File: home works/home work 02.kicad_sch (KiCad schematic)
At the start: 4 parts, among them U1 AW9523B, U2 XS2184, U3 BL0910, U4 HLK-7628N

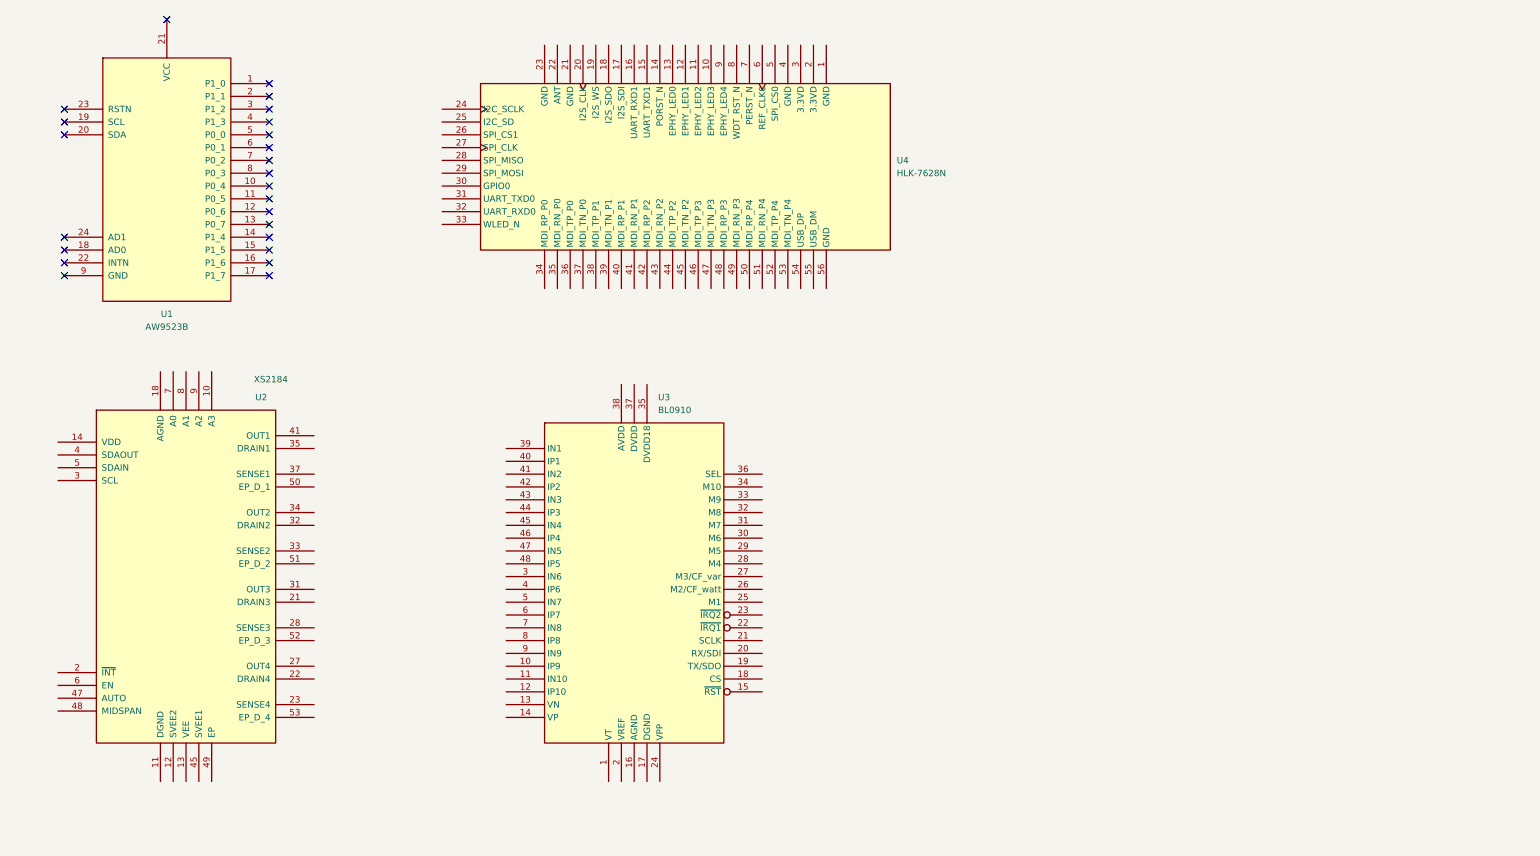
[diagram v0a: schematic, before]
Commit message: update schemas structure
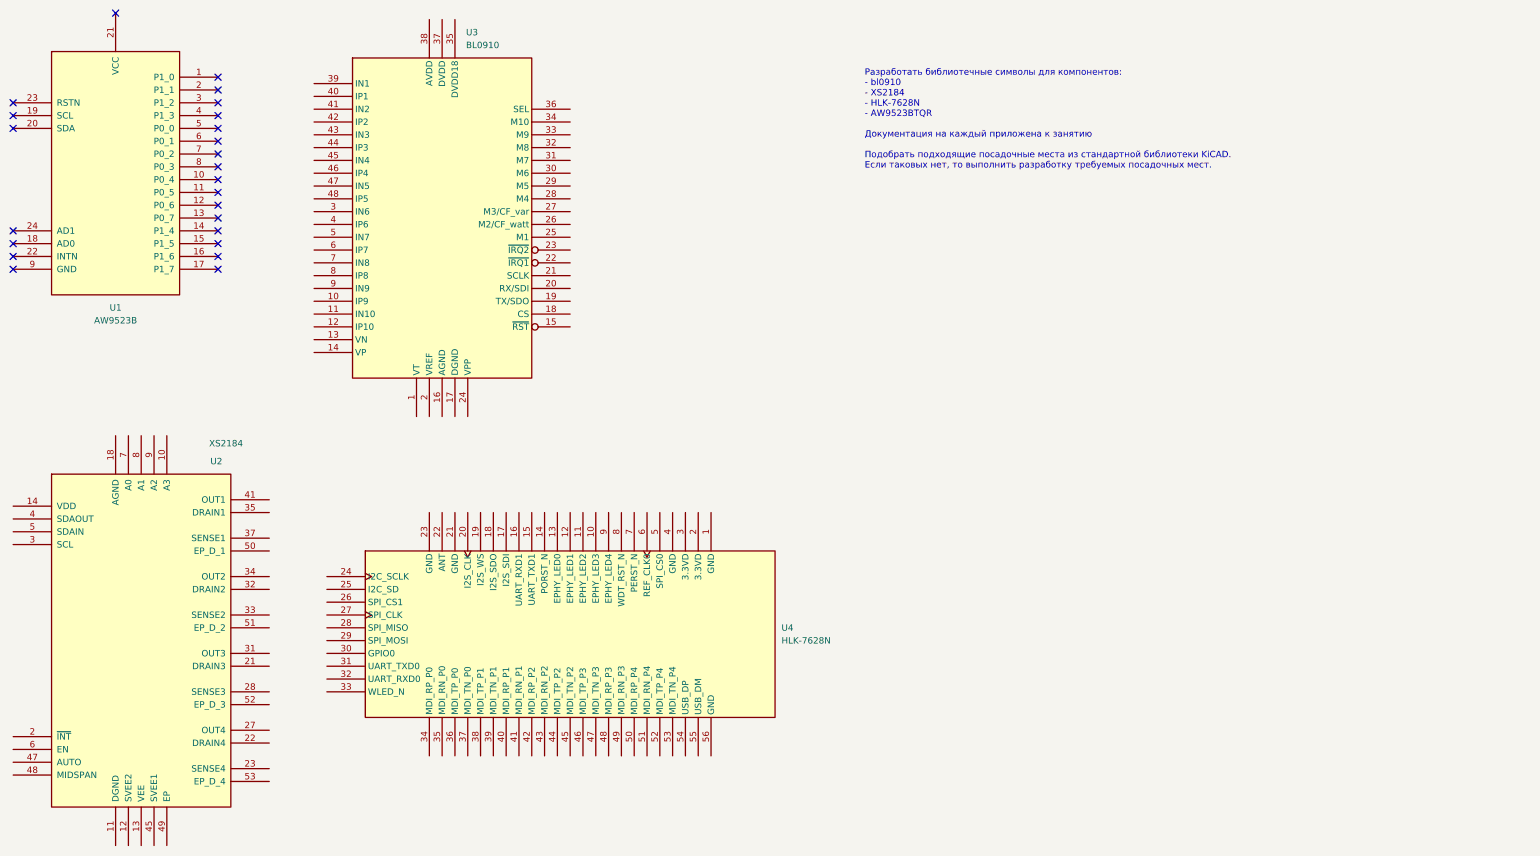
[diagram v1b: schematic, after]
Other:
- note added: "Разработать библиотечные символы для компонентов: - bl0910 - XS2184 - HLK-7628N - AW9523BTQR Документация на каждый приложена к занятию Подобрать подходящие посадочные места из стандартной библиотеки KiCAD. Если таковых нет, то выполнить разработку требуемых посадочных мест."
- moved on the sheet: U1, U2, U3, U4
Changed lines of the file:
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@@
 	(paper "A4")
 	(no_connect
-		(at 71.12 66.04)
-	)
-	(no_connect
-		(at 71.12 53.34)
-	)
-	(no_connect
-		(at 30.48 71.12)
-	)
-	(no_connect
-		(at 71.12 55.88)
-	)
-	(no_connect
-		(at 71.12 35.56)
-	)
-	(no_connect
-		(at 50.8 20.32)
-	)
-	(no_connect
-		(at 30.48 40.64)
-	)
-	(no_connect
-		(at 71.12 45.72)
-	)
-	(no_connect
-		(at 30.48 43.18)
-	)
-	(no_connect
-		(at 30.48 38.1)
-	)
-	(no_connect
-		(at 30.48 66.04)
-	)
-	(no_connect
-		(at 30.48 63.5)
-	)
-	(no_connect
-		(at 71.12 43.18)
-	)
-	(no_connect
-		(at 71.12 48.26)
-	)
-	(no_connect
-		(at 71.12 33.02)
-	)
-	(no_connect
-		(at 71.12 63.5)
-	)
-	(no_connect
-		(at 71.12 38.1)
-	)
-	(no_connect
-		(at 71.12 50.8)
-	)
-	(no_connect
-		(at 71.12 58.42)
-	)
-	(no_connect
-		(at 71.12 68.58)
-	)
-	(no_connect
-		(at 71.12 71.12)
-	)
-	(no_connect
-		(at 30.48 68.58)
-	)
-	(no_connect
-		(at 71.12 40.64)
-	)
-	(no_connect
-		(at 71.12 60.96)
+		(at 60.96 64.77)
+	)
+	(no_connect
+		(at 60.96 52.07)
+	)
+	(no_connect
+		(at 20.32 69.85)
+	)
+	(no_connect
+		(at 60.96 54.61)
+	)
+	(no_connect
+		(at 60.96 34.29)
+	)
+	(no_connect
+		(at 40.64 19.05)
+	)
+	(no_connect
+		(at 20.32 39.37)
+	)
+	(no_connect
+		(at 60.96 44.45)
+	)
+	(no_connect
+		(at 20.32 41.91)
+	)
+	(no_connect
+		(at 20.32 36.83)
+	)
+	(no_connect
+		(at 20.32 64.77)
+	)
+	(no_connect
+		(at 20.32 62.23)
+	)
+	(no_connect
+		(at 60.96 41.91)
+	)
+	(no_connect
+		(at 60.96 46.99)
+	)
+	(no_connect
+		(at 60.96 31.75)
+	)
+	(no_connect
+		(at 60.96 62.23)
+	)
+	(no_connect
+		(at 60.96 36.83)
+	)
+	(no_connect
+		(at 60.96 49.53)
+	)
+	(no_connect
+		(at 60.96 57.15)
+	)
+	(no_connect
+		(at 60.96 67.31)
+	)
+	(no_connect
+		(at 60.96 69.85)
+	)
+	(no_connect
+		(at 20.32 67.31)
+	)
+	(no_connect
+		(at 60.96 39.37)
+	)
+	(no_connect
+		(at 60.96 59.69)
+	)
+	(text "Разработать библиотечные символы для компонентов:\n- bl0910\n- XS2184\n- HLK-7628N\n- AW9523BTQR\n\nДокументация на каждый приложена к занятию\n\nПодобрать подходящие посадочные места из стандартной библиотеки KiCAD. \nЕсли таковых нет, то выполнить разработку требуемых посадочных мест. \n"
+		(exclude_from_sim no)
+		(at 189.23 40.132 0)
+		(effects
+			(font
+				(size 1.27 1.27)
+			)
+			(justify left)
+		)
 	)
 	(symbol
 		(lib_id "mipt:XS2184")
-		(at 54.61 130.81 0)
+		(at 45.72 143.51 0)
 		(unit 1)
 		(exclude_from_sim no)
@@
 		(dnp no)
 		(property "Reference" "U2"
-			(at 68.326 95.25 0)
+			(at 59.436 107.95 0)
 			(effects
 				(font
@@
 		)
 		(property "Value" "XS2184"
-			(at 68.072 91.694 0)
+			(at 59.182 104.394 0)
 			(effects
 				(font
@@
 		)
 		(property "Footprint" "mipt:QFN-48-1EP_7x7mm_P0.5mm_EP5.6x5.6mm_1"
-			(at 54.61 130.81 0)
+			(at 45.72 143.51 0)
 			(effects
 				(font
@@
 		)
 		(property "Datasheet" "./datasheets/XS2184 Datasheet CN V1.0.pdf"
-			(at 94.488 99.314 0)
+			(at 85.598 112.014 0)
 			(effects
 				(font
@@
 		)
 		(property "Description" ""
-			(at 54.61 130.81 0)
+			(at 45.72 143.51 0)
 			(effects
 				(font
@@
 	(symbol
 		(lib_id "mipt:HLK-7628N")
-		(at 153.67 49.53 0)
+		(at 130.81 142.24 0)
 		(unit 1)
 		(exclude_from_sim no)
@@
 		(fields_autoplaced yes)
 		(property "Reference" "U4"
-			(at 195.58 48.2599 0)
+			(at 172.72 140.9699 0)
 			(effects
 				(font
@@
 		)
 		(property "Value" "HLK-7628N"
-			(at 195.58 50.7999 0)
+			(at 172.72 143.5099 0)
 			(effects
 				(font
@@
 		)
 		(property "Footprint" "mipt:HLK-7628N"
-			(at 153.67 49.53 0)
+			(at 130.81 142.24 0)
 			(effects
 				(font
@@
 		)
 		(property "Datasheet" "./datasheets/HLK-7628N_V2.6.pdf"
-			(at 153.67 49.53 0)
+			(at 130.81 142.24 0)
 			(effects
 				(font
@@
 		)
 		(property "Description" ""
-			(at 153.67 49.53 0)
+			(at 130.81 142.24 0)
 			(effects
 				(font
@@
 	(symbol
 		(lib_id "mipt:AW9523B")
-		(at 50.8 52.07 0)
+		(at 40.64 50.8 0)
 		(unit 1)
 		(exclude_from_sim no)
@@
 		(fields_autoplaced yes)
 		(property "Reference" "U1"
-			(at 50.8 78.74 0)
+			(at 40.64 77.47 0)
 			(effects
 				(font
@@
 		)
 		(property "Value" "AW9523B"
-			(at 50.8 81.28 0)
+			(at 40.64 80.01 0)
 			(effects
 				(font
@@
 		)
 		(property "Footprint" "mipt:TQFN-24-1EP_4x4mm_P0.5mm_EP2.1x2.1mm"
-			(at 50.8 52.07 0)
+			(at 40.64 50.8 0)
 			(effects
 				(font
@@
 		)
 		(property "Datasheet" "./datasheets/AW9523+English+Datasheet.pdf"
-			(at 96.52 19.304 0)
+			(at 86.36 18.034 0)
 			(effects
 				(font
@@
 		)
 		(property "Description" ""
-			(at 50.8 52.07 0)
+			(at 40.64 50.8 0)
 			(effects
 				(font
@@
 	(symbol
 		(lib_id "mipt:bl0910")
-		(at 143.51 129.54 0)
+		(at 105.41 57.15 0)
 		(unit 1)
 		(exclude_from_sim no)
@@
 		(fields_autoplaced yes)
 		(property "Reference" "U3"
-			(at 148.2441 95.25 0)
+			(at 110.1441 22.86 0)
 			(effects
 				(font
@@
 		)
 		(property "Value" "BL0910"
-			(at 148.2441 97.79 0)
+			(at 110.1441 25.4 0)
 			(effects
 				(font
@@
 		)
 		(property "Footprint" "Package_QFP:LQFP-48_7x7mm_P0.5mm"
-			(at 182.88 90.678 0)
+			(at 144.78 18.288 0)
 			(effects
 				(font
@@
 		)
 		(property "Datasheet" "./datasheets/bl0910.pdf"
-			(at 176.022 95.25 0)
+			(at 137.922 22.86 0)
 			(effects
 				(font
@@
 		)
 		(property "Description" ""
-			(at 143.51 129.54 0)
-			(effects
-				(font
+			(at 105.41 57.15 0)
+			(effects
+				(font

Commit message: start home work 3. task 1
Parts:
- renumbered U3 to U2, U4 to U3, U2 to U4
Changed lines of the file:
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@@
 		(on_board yes)
 		(dnp no)
-		(property "Reference" "U2"
+		(property "Reference" "U4"
 			(at 59.436 107.95 0)
 			(effects
@@
 			(project "mipt"
 				(path "/34d483ea-61c1-4e08-b30a-5dee616d4777/c73feff7-a444-4fc1-b029-86822a883591"
-					(reference "U2")
+					(reference "U4")
 					(unit 1)
 				)
@@
 		(dnp no)
 		(fields_autoplaced yes)
-		(property "Reference" "U4"
+		(property "Reference" "U3"
 			(at 172.72 140.9699 0)
 			(effects
@@
 			(project "mipt"
 				(path "/34d483ea-61c1-4e08-b30a-5dee616d4777/c73feff7-a444-4fc1-b029-86822a883591"
-					(reference "U4")
+					(reference "U3")
 					(unit 1)
 				)
@@
 		(dnp no)
 		(fields_autoplaced yes)
-		(property "Reference" "U3"
+		(property "Reference" "U2"
 			(at 110.1441 22.86 0)
 			(effects
@@
 			(project "mipt"
 				(path "/34d483ea-61c1-4e08-b30a-5dee616d4777/c73feff7-a444-4fc1-b029-86822a883591"
-					(reference "U3")
+					(reference "U2")
 					(unit 1)
 				)
